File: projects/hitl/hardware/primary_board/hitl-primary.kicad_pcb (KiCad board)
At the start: 4 copper layers, 108 x 79.7 mm, 135 parts, among them J1 USB-Micro-1981568-1, J10 CONN_01X03, J11 CONN_01X03, J12 CONN_01X03, J13 CONN_01x02, J14 SSW-122-01-G-D, J15 CONN_01x02, J16 CONN_01X03, J17 CONN_01X03, J18 CONN_01X03, J19 CONN_01X03, J2 Barrel_jack, J20 CONN_01X03, J21 Screw_Terminal_01x03, J3 MM_F_VT_08_SM, J4 MM_F_VT_08_SM, J6 CONN_01x02, J7 CONN_01X03, J8 CONN_01X03, J9 CONN_01X03, Q1 SSM3K333R, Q2 SSM3K333R, Q3 SSM3K333R, Q4 SSM3K333R, SW1 SW_SPST, U1 PCA9517, U2 FT4222H, U4 AD5675, U5 MAX7300AAXT, U6 AD7091R-5BRUZ, U7 MCP6001, U8 74HCT4051D, U9 LT3045, Y1 Crystal_12MHz

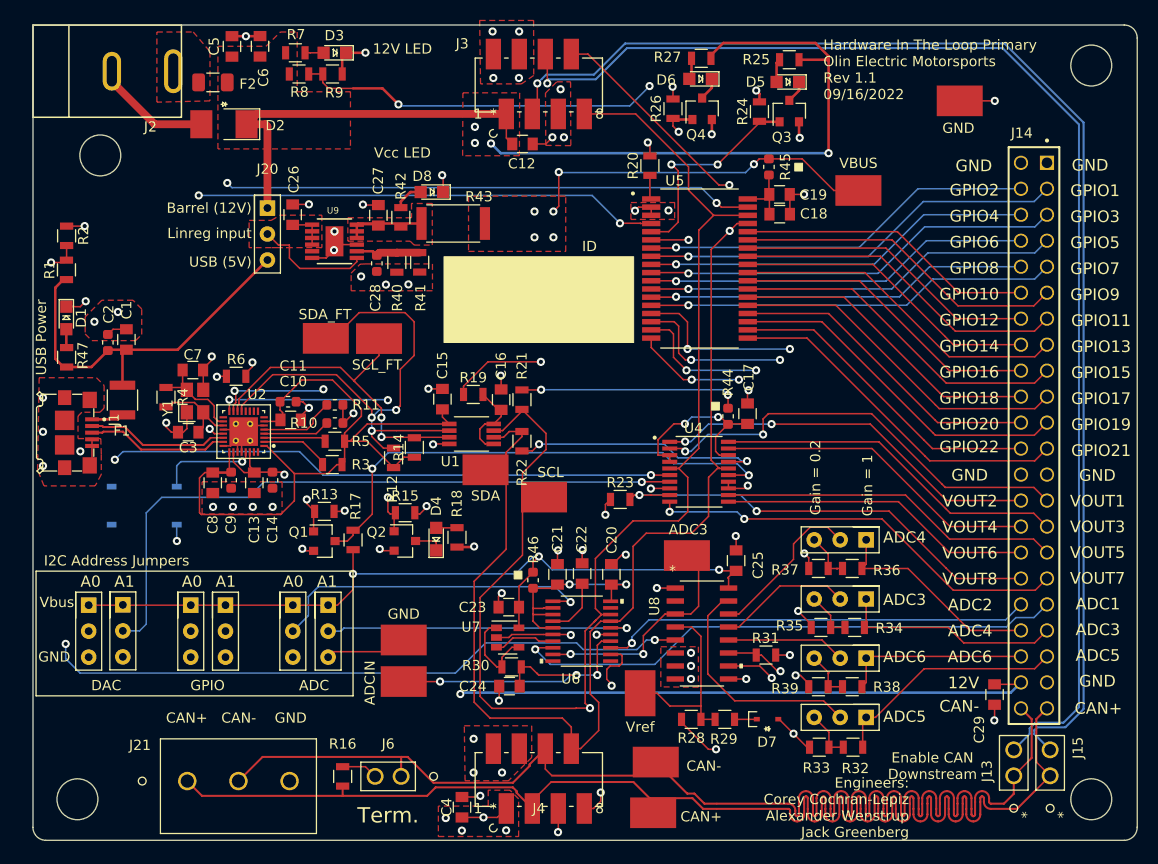
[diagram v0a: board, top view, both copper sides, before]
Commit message: Fix footprint for FTDI chip
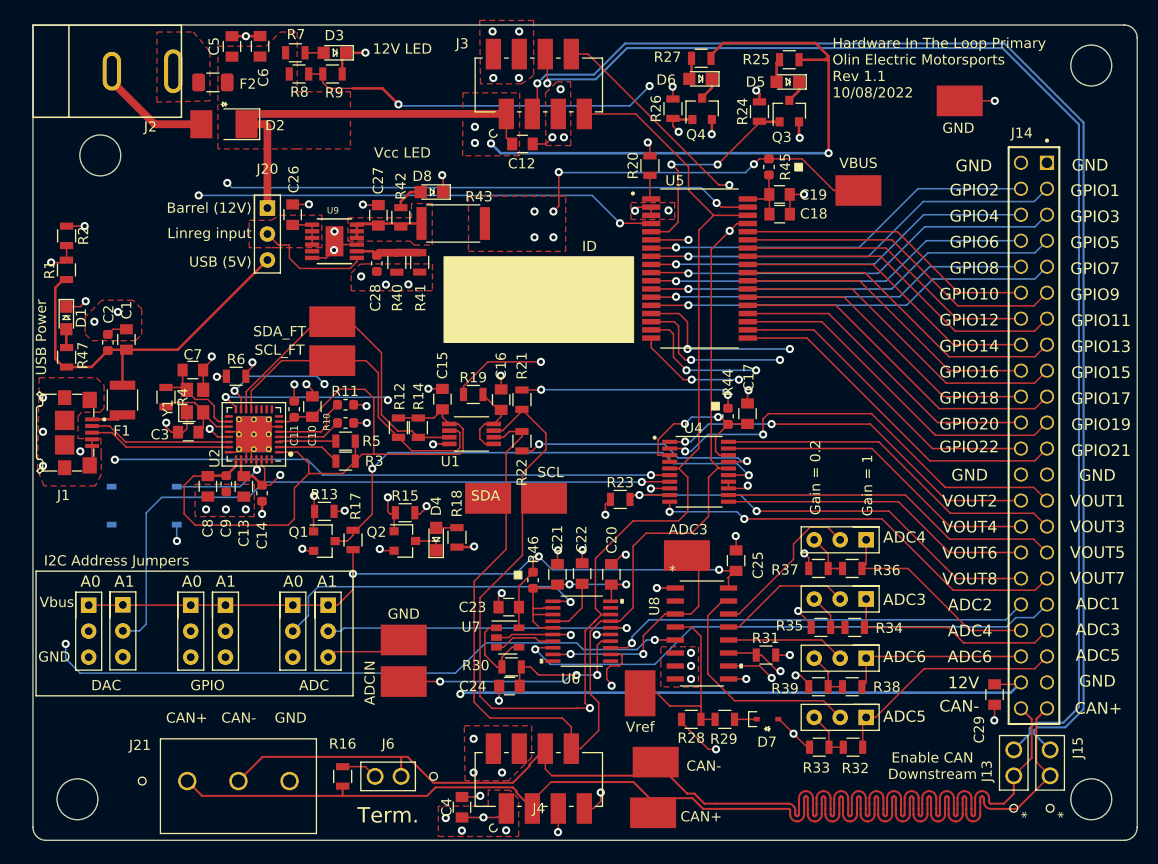
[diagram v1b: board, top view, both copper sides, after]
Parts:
- QR*****: footprint qr.olinelectricmotorsports.com/hw/hitl/1.1 -> qr.olinelectricmotorsports.com_hw_hitl_1.1
- U2: footprint footprints:FT4222_QFN -> Package_DFN_QFN:VQFN-32-1EP_5x5mm_P0.5mm_EP3.5x3.5mm_ThermalVias
- moved TP5 4.86 mm to (101.9, 63.5)
- moved R12 2.99 mm to (108.3, 73.9), turned to -90 degrees
- moved TP6 2.81 mm to (117.1, 80.8)
- moved C10 2.49 mm to (99.9, 71.8), turned to 90 degrees
- moved TP4 2.27 mm to (101.9, 67.3)
- moved R14 1.97 mm to (110.3, 73.9), turned to -90 degrees
- moved C14 1.63 mm to (95.0, 80.3)
- moved R3 1.35 mm to (103.2, 77.1)
- moved C13 1.08 mm to (93.2, 79.6)
- moved R10 1.05 mm to (103.2, 73.4)
- moved R11 1.05 mm to (103.2, 71.6)
- moved R5 1.05 mm to (103.2, 75.2)
- moved U2 1.03 mm to (94.2, 74.5)
- moved C11 0.94 mm to (98.1, 72.1), turned to 90 degrees
- moved C9 0.59 mm to (91.5, 79.3)
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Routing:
- net /USB->I2C/SDA: track 50.8 -> 32.3 mm, vias 3 -> 0
- net +3V3: track 71.3 -> 74.5 mm
- net /Connectors/SDA: track 137.5 -> 134.9 mm
- net +5V: track 67.8 -> 69.0 mm
- net Net-(Q2-Pad1): track 30.1 -> 31.1 mm
- net /DAC/DAC-LDAC: track 25.8 -> 26.9 mm
- net GND: track 137.0 -> 138.0 mm, vias 73 -> 75
- net Net-(R3-Pad1): track 6.81 -> 6.14 mm
- net Net-(R6-Pad1): track 8.10 -> 8.77 mm
- net /DAC/DAC-A0: track 73.3 -> 72.7 mm
- net Net-(C3-Pad1): track 8.66 -> 9.25 mm
- net Net-(C7-Pad1): track 9.80 -> 10.4 mm
- net Net-(R5-Pad1): track 6.11 -> 5.60 mm
- net /USB->I2C/SCL: vias 2 -> 0
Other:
- board text added: "Hardware In The Loop Primary Olin Electric Motorsports Rev 1.1 10/08/2022"
- board text removed: "Engineers: Corey Cochran-Lepiz Alexander Wenstrup Jack Greenberg"
- board text removed: "Hardware In The Loop Primary Olin Electric Motorsports Rev 1.1 09/16/2022"

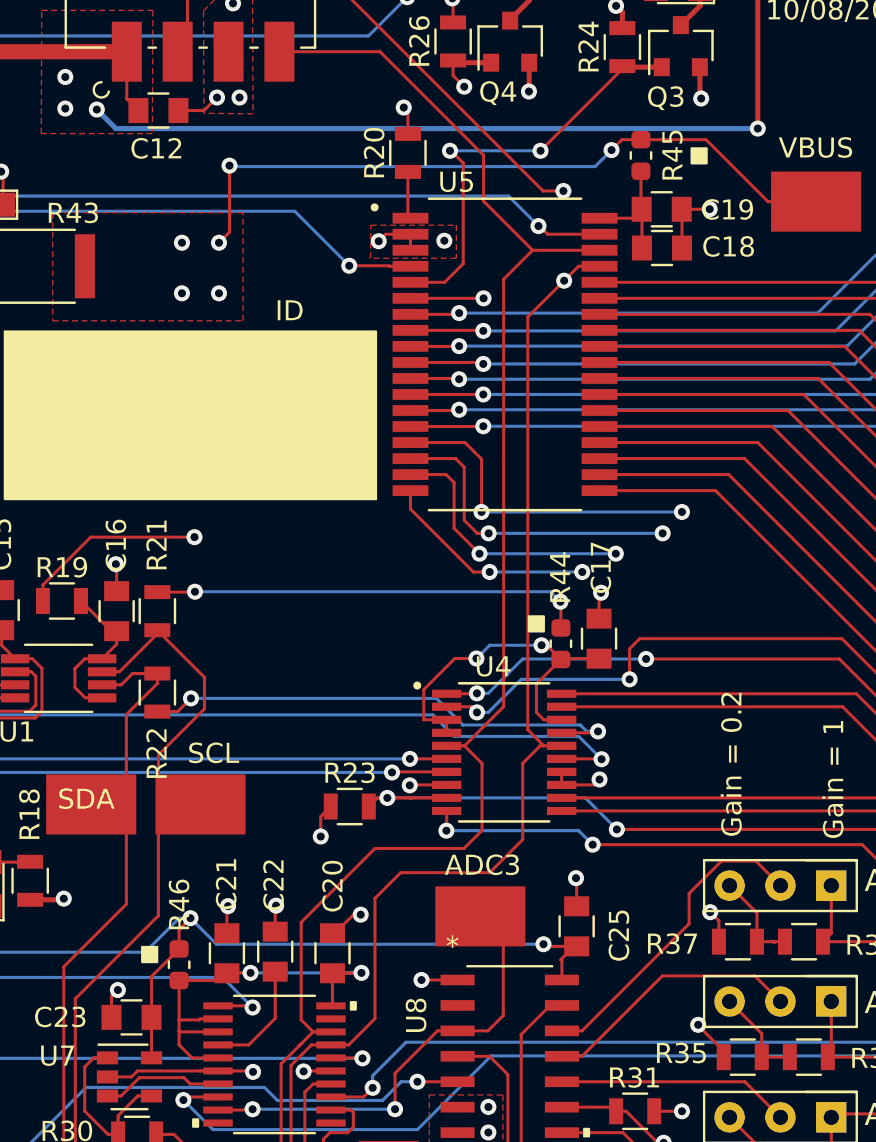
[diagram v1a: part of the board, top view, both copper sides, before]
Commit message: Replace zero-ohm resistors with solder jumpers
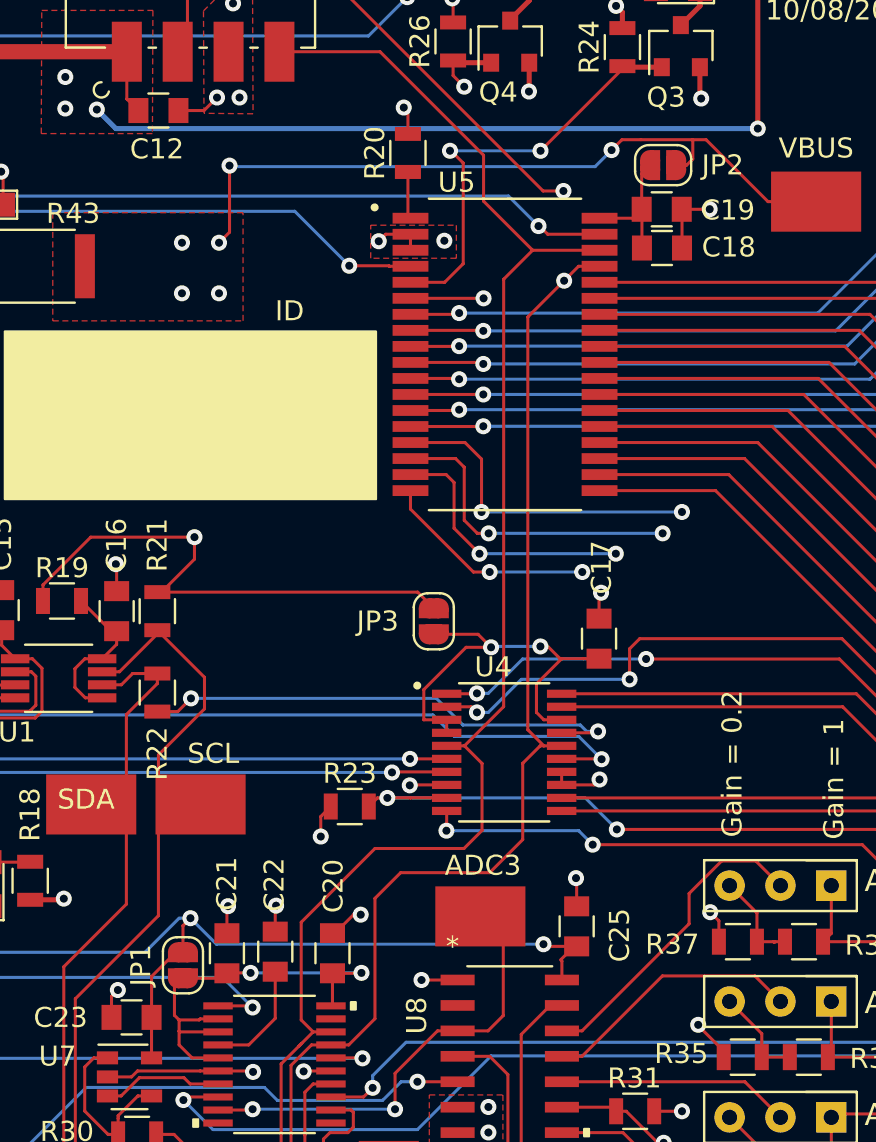
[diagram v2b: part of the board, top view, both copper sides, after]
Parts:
- removed G***: LOGO, footprints:Small_OE_Logo
- removed QR*****: Scan for docs, qr.olinelectricmotorsports.com_hw_hitl_1.1
- removed R44, R45, R46: R_0, footprints:R_0603_1608Metric
- added JP1: SolderJumper_2_Open, Jumper:SolderJumper-2_P1.3mm_Open_RoundedPad1.0x1.5mm, F.Cu at (121.7, 88.8)
- added JP2: SolderJumper_2_Open, Jumper:SolderJumper-2_P1.3mm_Open_RoundedPad1.0x1.5mm, F.Cu at (145.7, 48.9)
- added JP3: SolderJumper_2_Open, Jumper:SolderJumper-2_P1.3mm_Open_RoundedPad1.0x1.5mm, F.Cu at (134.2, 71.6)
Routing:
- net Net-(C17-Pad1): track 17.8 -> 20.9 mm
- net VBUS: track 192.5 -> 190.5 mm, vias 15 -> 13
- net Net-(C18-Pad1): track 6.14 -> 6.66 mm

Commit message: Changes from feedback
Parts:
- removed D2: D_Zener_13V, footprints:D_13V_Zener
- added D501: D_Zener_18V, footprints:DO-214AA, F.Cu at (91.4, 44.2)
- added R401: R_1K, footprints:R_0805_OEM, F.Cu at (96.8, 81.3)
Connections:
- SW1 pad 3: GND -> Net-(R401-Pad2)
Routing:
- net Net-(R401-Pad2): track 0.00 -> 13.4 mm, vias 0 -> 1
- net +5V: track 69.0 -> 71.2 mm
- net GND: track 138.0 -> 136.4 mm
- net (no net): vias 2 -> 0

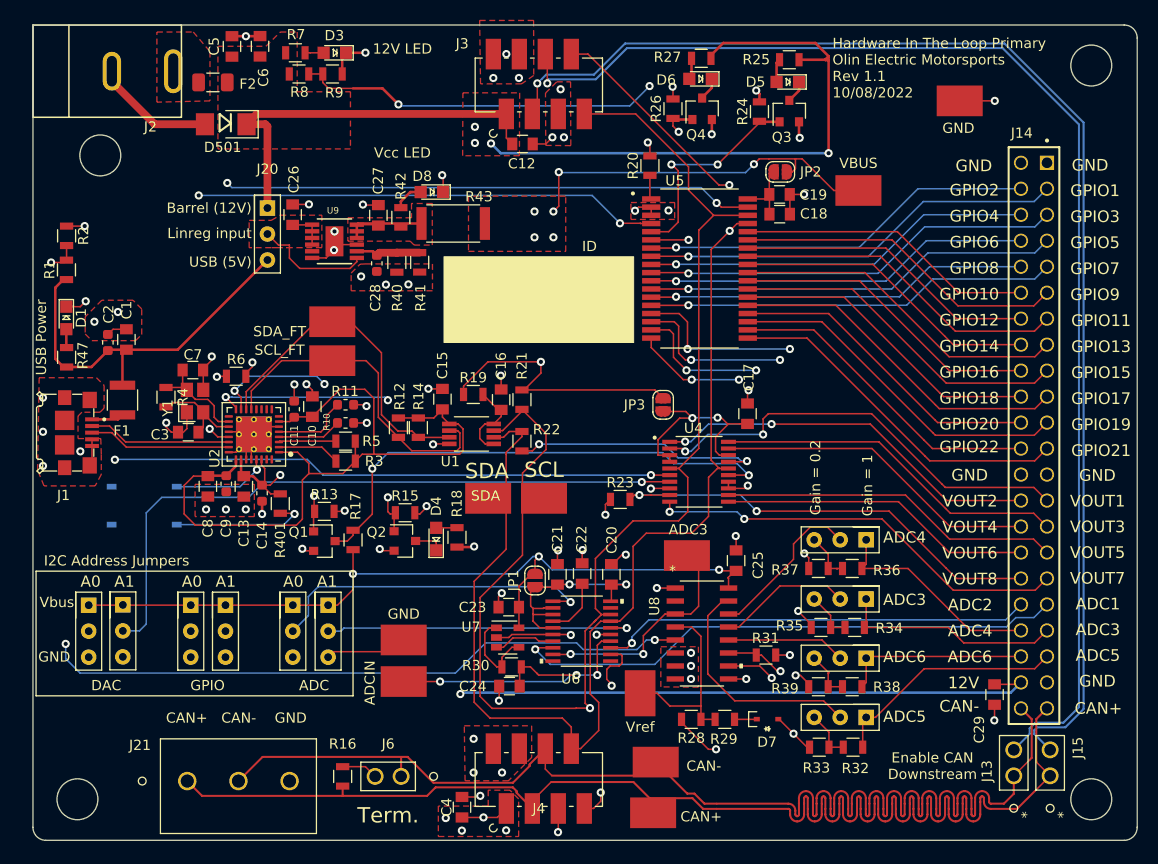
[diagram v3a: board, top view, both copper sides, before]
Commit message: Finalize boards for fab (#217)
* add BOM tool to join BOMs

* add custom BOM script for working with custom BOM fields

* add patched QR plugin for better QR codes

* add logo and authors to boards

* update parts library and fix misc issues

* migrate projects to new parts library
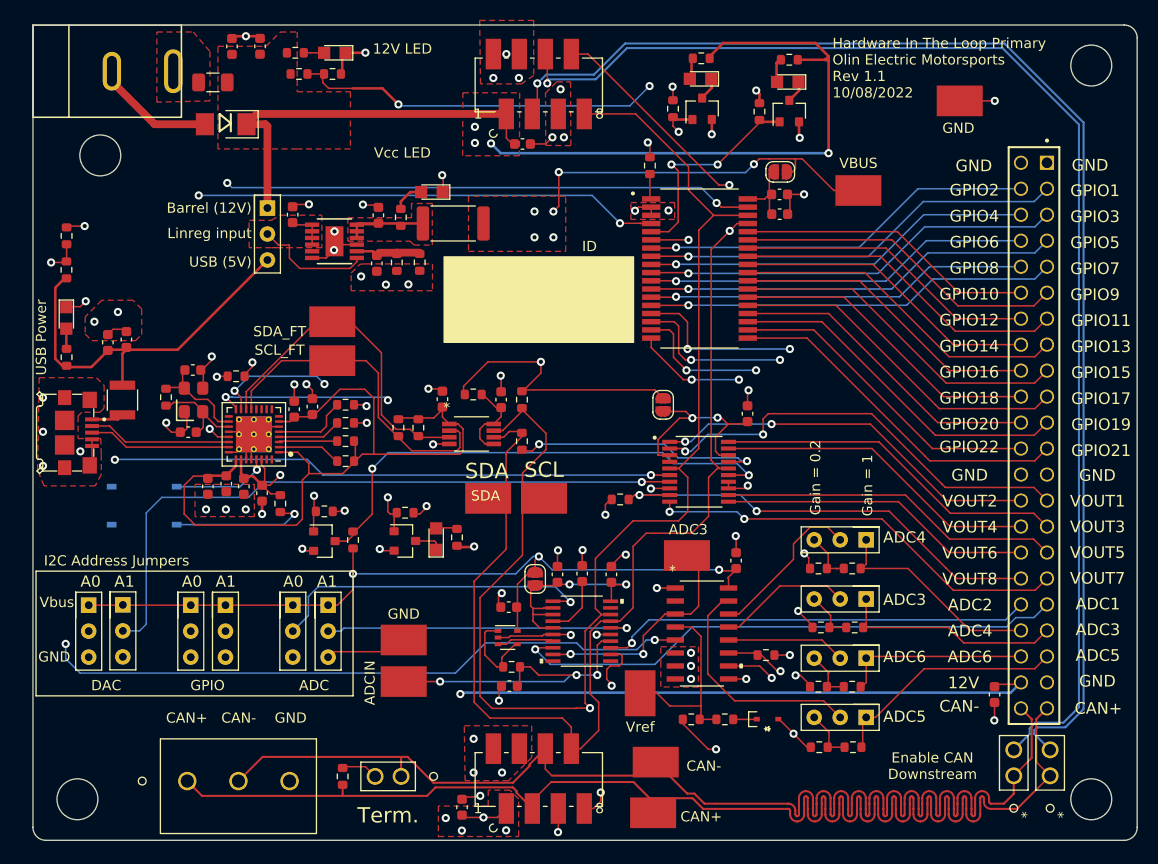
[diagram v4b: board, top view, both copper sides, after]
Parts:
- C1, C10, C13, C15, C26, C8: value C_4.7uF_25V -> 4u7F; footprint footprints:C_0805_OEM -> OEM:C_0603
- C11, C14, C2, C9: value C_100nF -> 0u1F; footprint footprints:C_0603_1608Metric -> OEM:C_0603
- C12, C29, C4, C5, C6: value C_10uF_50V -> 10uF_35V; footprint footprints:C_0805_OEM -> OEM:C_0603
- C16: value C_100pF -> 0u1F; footprint footprints:C_0805_OEM -> OEM:C_0603
- C17, C20: value C_10uF_16V -> 10uF_35V; footprint footprints:C_0805_OEM -> OEM:C_0603
- C18, C25: value C_0.1uF -> 0u1F; footprint footprints:C_0805_OEM -> OEM:C_0603
- C19, C27: value C_10uF_25V -> 10uF_35V; footprint footprints:C_0805_OEM -> OEM:C_0603
- C21: value C_2.2uF -> 2u2F; footprint footprints:C_0805_OEM -> OEM:C_0603
- C22, C23: value C_1uF -> 1uF; footprint footprints:C_0805_OEM -> OEM:C_0603
- C24, C3, C7: value C_30pF -> 30pF; footprint footprints:C_0805_OEM -> OEM:C_0603
- C28: value C_1000nF -> 1uF; footprint footprints:C_0603_1608Metric -> OEM:C_0603
- D1, D3, D8: value LED_0805 -> LED_WHITE; footprint footprints:LED_0805_OEM -> OEM:CHIPLED_0805
- D4: value LED_0805_Red -> LED_BLUE; footprint footprints:LED_0805_OEM -> OEM:CHIPLED_0805
- D5, D6: value LED_0805_Amber -> LED_ORANGE; footprint footprints:LED_0805_OEM -> OEM:CHIPLED_0805
- D501: value D_Zener_18V -> SMBJ5355B-TP
- D7: value D_Zener_2V -> GDZ2V0B-G3-08
- F2: value 1.5A_Fuse -> F_1500mA_63V
- J2: value Barrel_jack -> Barrel_Jack
- J3, J4: value MM_F_VT_08_SM -> CONN_MM_F_VT_08_SM
- Q1, Q2, Q3, Q4: footprint footprints:SOT-23F -> OEM:SOT-23F
- R1, R32, R34, R36, R38, R6, R8: value R_12K -> 12KR; footprint footprints:R_0805_OEM -> OEM:R_0603
- R10, R11: value R_0 -> 0R; footprint footprints:R_0603_1608Metric -> OEM:R_0603
- R12, R14, R21, R22: value R_8.06k -> 8K06R; footprint footprints:R_0805_OEM -> OEM:R_0603
- R13, R15, R17, R24, R26, R28, R29, R3, R31, R5: value R_10K -> 10KR; footprint footprints:R_0805_OEM -> OEM:R_0603
- R16: value R_120 -> 120R; footprint footprints:R_0805_OEM -> OEM:R_0603
- R18, R25, R27, R7: value R_1.91K -> 3KR; footprint footprints:R_0805_OEM -> OEM:R_0603
- R19: value R_200K -> 100KR; footprint footprints:R_0805_OEM -> OEM:R_0603
- R2, R33, R35, R37, R39, R9: value R_3.01K -> 3KR; footprint footprints:R_0805_OEM -> OEM:R_0603
- R20: value R_39K -> 39KR; footprint footprints:R_0805_OEM -> OEM:R_0603
- R23, R30, R401: value R_1K -> 1KR; footprint footprints:R_0805_OEM -> OEM:R_0603
- R4: value R_1M -> 1MR; footprint footprints:R_0805_OEM -> OEM:R_0603
- R40: value R_33.2k -> 33K2R; footprint footprints:R_0805_OEM -> OEM:R_0603
- R41: value R_49.90k -> 49K9R; footprint footprints:R_0805_OEM -> OEM:R_0603
- R42: value R_330 -> 330R; footprint footprints:R_0805_OEM -> OEM:R_0603
- R43: value R_0_2512 -> 0R_2512; footprint footprints:R_2512_OEM -> Resistor_SMD:R_2512_6332Metric
- R47: value R_500 -> 1KR; footprint footprints:R_0805_OEM -> OEM:R_0603
- TP1, TP10, TP11, TP12, TP2, TP3, TP4, TP5, TP6, TP7, TP8, TP9: value Test_Point_SMD -> TP_SMD
- U7: footprint footprints:SOT-23-5_OEM -> Package_TO_SOT_SMD:SOT-353_SC-70-5
- Y1: value Crystal_12MHz -> Crystal_12MHz_20pF; footprint footprints:Crystal_SMD_FA238 -> OEM:ECX-32
- moved Y1 0.19 mm to (88.3, 71.2)
- moved JP1 0.15 mm to (121.7, 88.7)
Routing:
- net Net-(U6-Pad7): track 6.03 -> 5.45 mm
